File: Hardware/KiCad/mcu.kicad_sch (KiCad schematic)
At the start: 12 parts, among them U3 STM32F427ZGTx, Y1 8 MHz, Y2 32 kHz

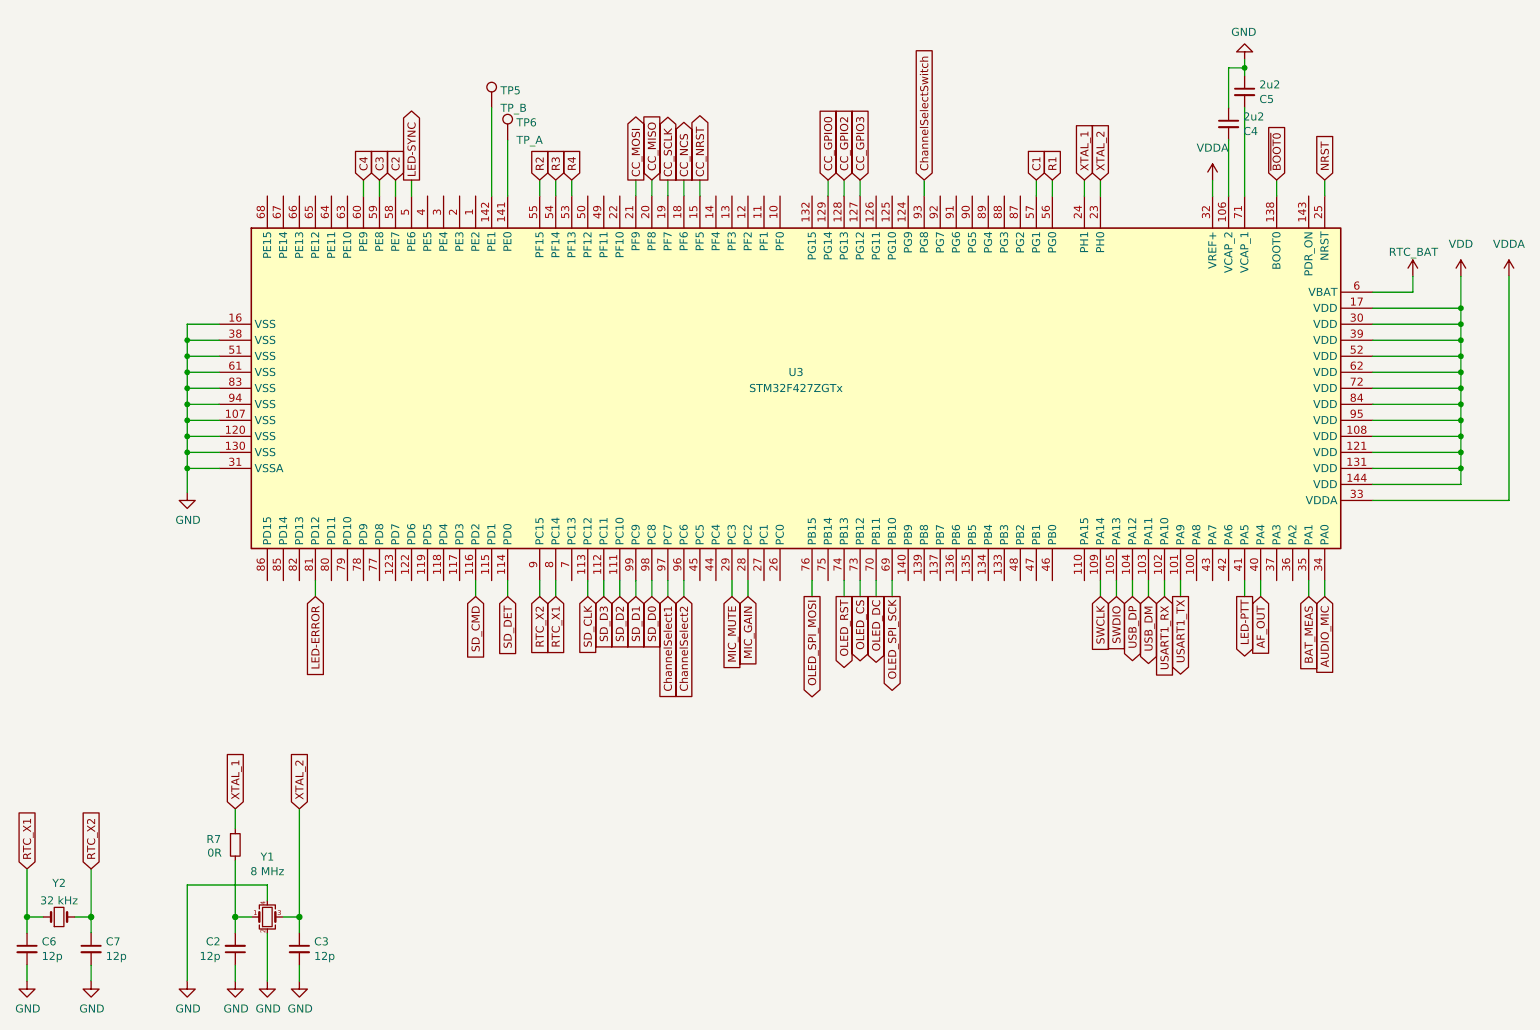
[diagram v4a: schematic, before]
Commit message: Schematic update
- nets for the internal speaker renamed
- encoder nets renamed, encoder circuit updated
- various other minor edits
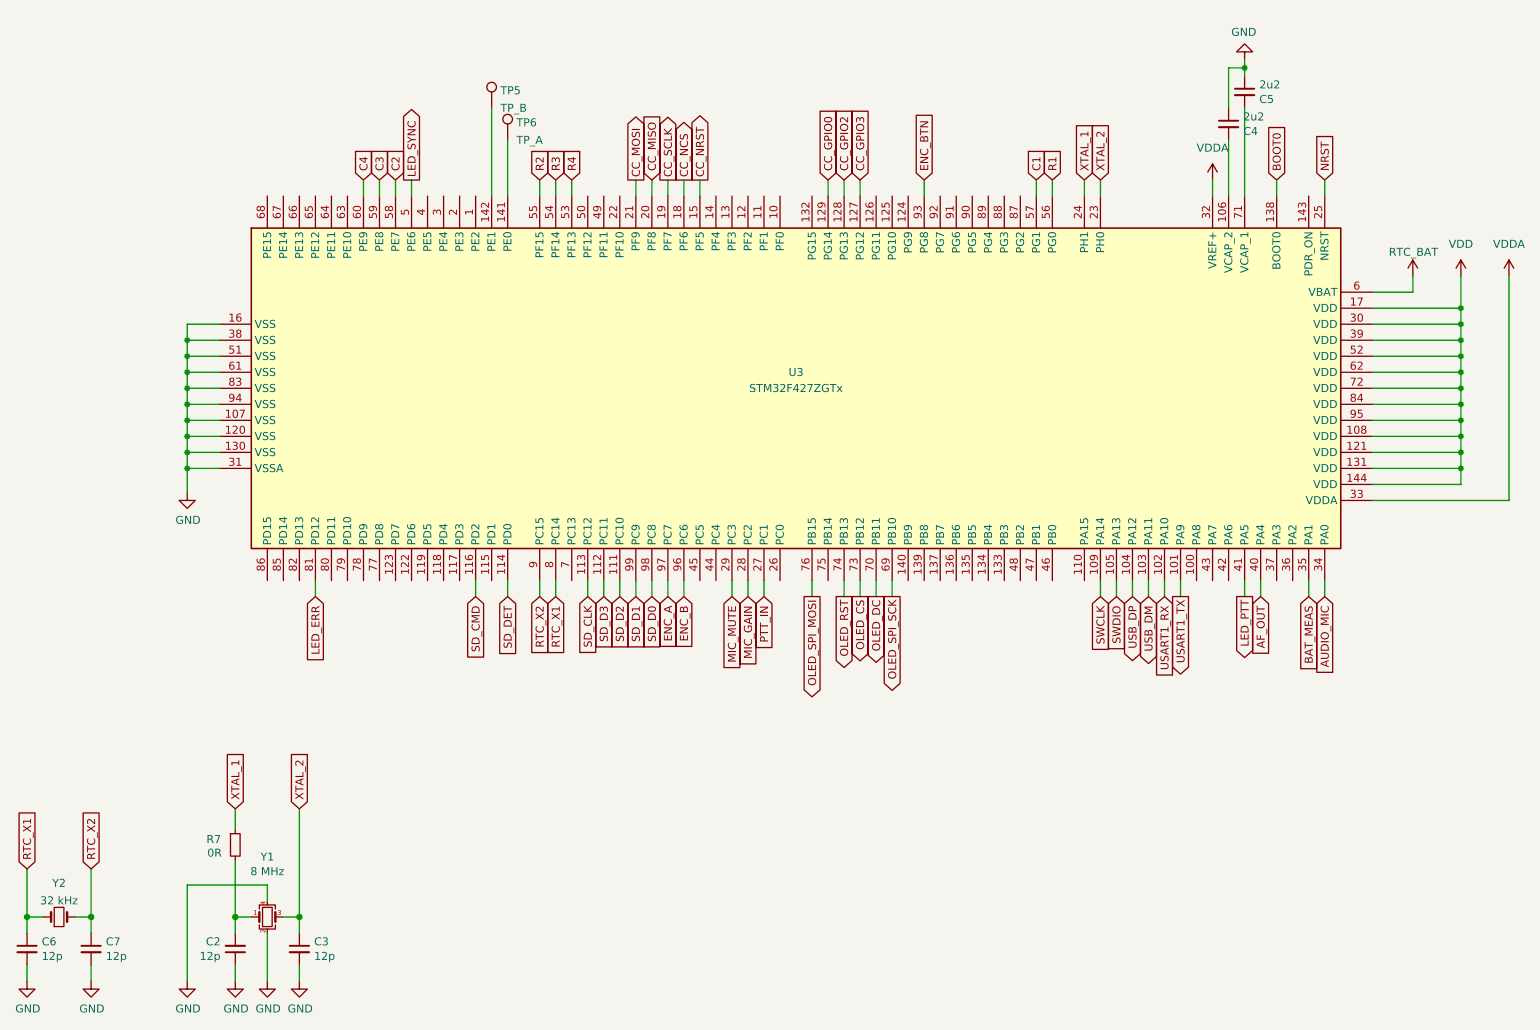
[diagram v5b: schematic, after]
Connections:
- net PTT_IN: now reaches U3.27 (PC1)
- net ChannelSelect1 renamed ENC_A
- net ChannelSelect2 renamed ENC_B
- net ChannelSelectSwitch renamed ENC_BTN
- net LED-ERROR renamed LED_ERR
- net LED-PTT renamed LED_PTT
- net LED-SYNC renamed LED_SYNC
- net ~{BOOT0} renamed BOOT0
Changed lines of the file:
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@@
+    (stroke (width 0) (type default) (color 0 0 0 0))
+  )
+  (wire (pts (xy 144.78 114.3) (xy 144.78 116.84))
     (stroke (width 0) (type default) (color 0 0 0 0))
   )
@@
     )
   )
-  (global_label "LED-SYNC" (shape output) (at 88.9 50.8 90) (fields_autoplaced)
-    (effects (font (size 1.27 1.27)) (justify left))
-    (property "Intersheet References" "${INTERSHEET_REFS}" (id 0) (at 88.8206 38.4688 90)
+  (global_label "LED_SYNC" (shape output) (at 88.9 50.8 90) (fields_autoplaced)
+    (effects (font (size 1.27 1.27)) (justify left))
+    (property "Intersheet References" "${INTERSHEET_REFS}" (id 0) (at 88.8206 39.0736 90)
       (effects (font (size 1.27 1.27)) (justify left) hide)
     )
@@
     )
   )
-  (global_label "LED-ERROR" (shape input) (at 73.66 116.84 270) (fields_autoplaced)
-    (effects (font (size 1.27 1.27)) (justify right))
-    (property "Intersheet References" "${INTERSHEET_REFS}" (id 0) (at -81.28 378.46 0)
-      (effects (font (size 1.27 1.27)) hide)
+  (global_label "LED_ERR" (shape input) (at 73.66 116.84 270) (fields_autoplaced)
+    (effects (font (size 1.27 1.27)) (justify right))
+    (property "Intersheet References" "${INTERSHEET_REFS}" (id 0) (at 73.5806 127.3569 90)
+      (effects (font (size 1.27 1.27)) (justify right) hide)
     )
   )
@@
     )
   )
-  (global_label "~{BOOT0}" (shape input) (at 226.06 50.8 90) (fields_autoplaced)
-    (effects (font (size 1.27 1.27)) (justify left))
-    (property "Intersheet References" "${INTERSHEET_REFS}" (id 0) (at 265.43 -19.05 0)
-      (effects (font (size 1.27 1.27)) hide)
+  (global_label "BOOT0" (shape input) (at 226.06 50.8 90) (fields_autoplaced)
+    (effects (font (size 1.27 1.27)) (justify left))
+    (property "Intersheet References" "${INTERSHEET_REFS}" (id 0) (at 225.9806 42.2788 90)
+      (effects (font (size 1.27 1.27)) (justify left) hide)
     )
   )
@@
     )
   )
-  (global_label "ChannelSelect1" (shape input) (at 129.54 116.84 270) (fields_autoplaced)
-    (effects (font (size 1.27 1.27)) (justify right))
-    (property "Intersheet References" "${INTERSHEET_REFS}" (id 0) (at 129.4606 133.9488 90)
+  (global_label "ENC_A" (shape input) (at 129.54 116.84 270) (fields_autoplaced)
+    (effects (font (size 1.27 1.27)) (justify right))
+    (property "Intersheet References" "${INTERSHEET_REFS}" (id 0) (at 129.4606 125.0588 90)
       (effects (font (size 1.27 1.27)) (justify right) hide)
     )
@@
     )
   )
-  (global_label "LED-PTT" (shape output) (at 220.98 116.84 270) (fields_autoplaced)
-    (effects (font (size 1.27 1.27)) (justify right))
-    (property "Intersheet References" "${INTERSHEET_REFS}" (id 0) (at 220.9006 127.4779 90)
+  (global_label "LED_PTT" (shape output) (at 220.98 116.84 270) (fields_autoplaced)
+    (effects (font (size 1.27 1.27)) (justify right))
+    (property "Intersheet References" "${INTERSHEET_REFS}" (id 0) (at 220.9006 126.8731 90)
       (effects (font (size 1.27 1.27)) (justify right) hide)
     )
@@
     )
   )
-  (global_label "ChannelSelect2" (shape input) (at 132.08 116.84 270) (fields_autoplaced)
-    (effects (font (size 1.27 1.27)) (justify right))
-    (property "Intersheet References" "${INTERSHEET_REFS}" (id 0) (at 132.0006 133.9488 90)
+  (global_label "ENC_B" (shape input) (at 132.08 116.84 270) (fields_autoplaced)
+    (effects (font (size 1.27 1.27)) (justify right))
+    (property "Intersheet References" "${INTERSHEET_REFS}" (id 0) (at 132.0006 125.2402 90)
       (effects (font (size 1.27 1.27)) (justify right) hide)
     )
@@
     )
   )
-  (global_label "ChannelSelectSwitch" (shape input) (at 170.18 50.8 90) (fields_autoplaced)
-    (effects (font (size 1.27 1.27)) (justify left))
-    (property "Intersheet References" "${INTERSHEET_REFS}" (id 0) (at 170.1006 28.7926 90)
+  (global_label "ENC_BTN" (shape input) (at 170.18 50.8 90) (fields_autoplaced)
+    (effects (font (size 1.27 1.27)) (justify left))
+    (property "Intersheet References" "${INTERSHEET_REFS}" (id 0) (at 170.1006 40.1017 90)
       (effects (font (size 1.27 1.27)) (justify left) hide)
     )
@@
     )
   )
+  (global_label "PTT_IN" (shape input) (at 144.78 116.84 270) (fields_autoplaced)
+    (effects (font (size 1.27 1.27)) (justify right))
+    (property "Intersheet References" "${INTERSHEET_REFS}" (id 0) (at 144.8594 125.3612 90)
+      (effects (font (size 1.27 1.27)) (justify right) hide)
+    )
+  )

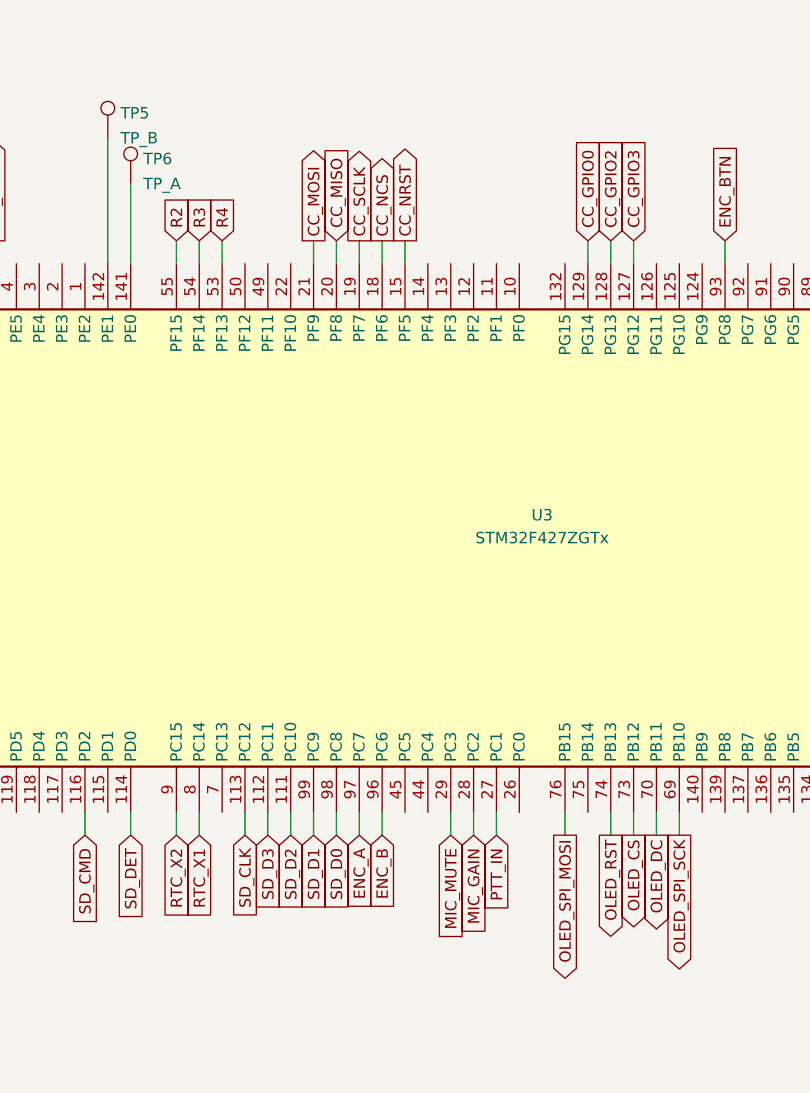
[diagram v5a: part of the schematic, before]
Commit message: Additional function buttons - F1, F2
Closes #24
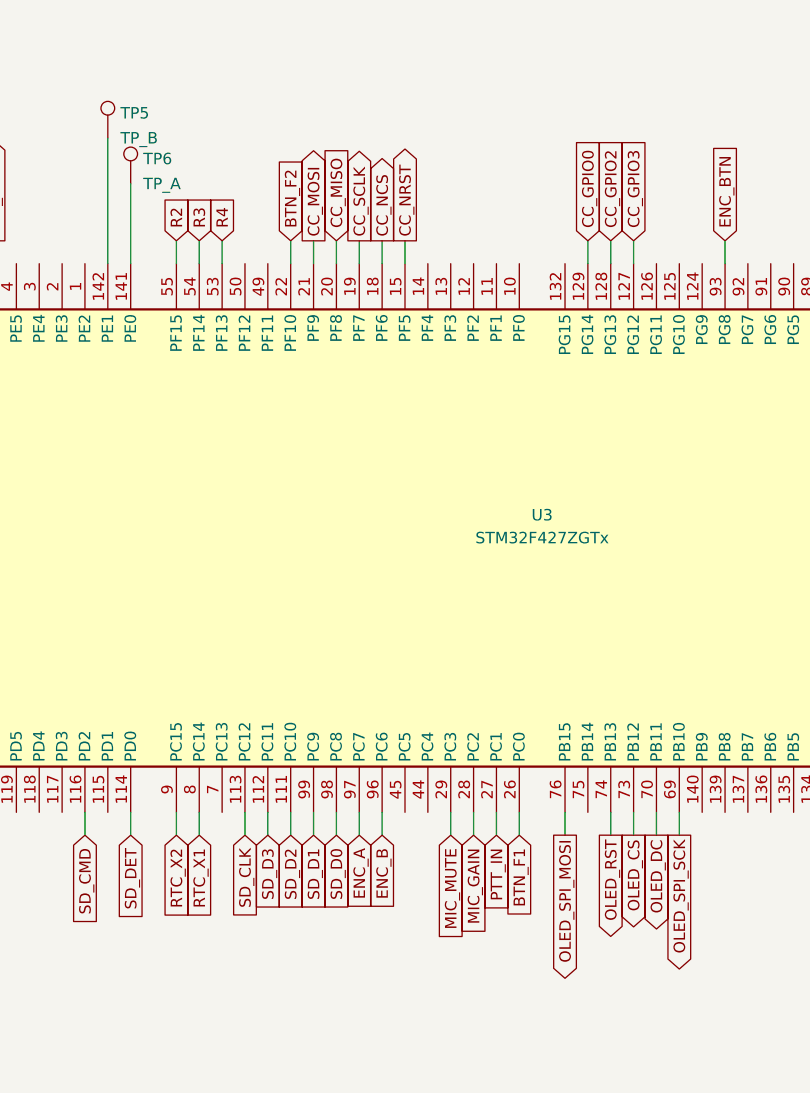
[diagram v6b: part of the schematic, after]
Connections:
- net BTN_F2: now reaches U3.22 (PF10)
- net BTN_F1: now reaches U3.26 (PC0)
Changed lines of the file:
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@@
+    (stroke (width 0) (type default) (color 0 0 0 0))
+  )
+  (wire (pts (xy 147.32 114.3) (xy 147.32 116.84))
     (stroke (width 0) (type default) (color 0 0 0 0))
   )
@@
     (stroke (width 0) (type default) (color 0 0 0 0))
   )
+  (wire (pts (xy 121.92 50.8) (xy 121.92 53.34))
+    (stroke (width 0) (type default) (color 0 0 0 0))
+  )
   (wire (pts (xy 241.3 76.2) (xy 255.27 76.2))
     (stroke (width 0) (type default) (color 0 0 0 0))
@@
     (effects (font (size 1.27 1.27)) (justify left))
     (property "Intersheet References" "${INTERSHEET_REFS}" (id 0) (at 134.5406 40.1017 90)
+      (effects (font (size 1.27 1.27)) (justify left) hide)
+    )
+  )
+  (global_label "BTN_F2" (shape input) (at 121.92 50.8 90) (fields_autoplaced)
+    (effects (font (size 1.27 1.27)) (justify left))
+    (property "Intersheet References" "${INTERSHEET_REFS}" (id 0) (at 121.8406 41.5531 90)
       (effects (font (size 1.27 1.27)) (justify left) hide)
     )
@@
       (effects (font (size 1.27 1.27)) (justify right) hide)
     )
+  )
+  (global_label "BTN_F1" (shape input) (at 147.32 116.84 270) (fields_autoplaced)
+    (effects (font (size 1.27 1.27)) (justify right))
+    (property "Intersheet References" "${INTERSHEET_REFS}" (id 0) (at 147.2406 126.0869 90)
+      (effects (font (size 1.27 1.27)) (justify right) hide)
+    )

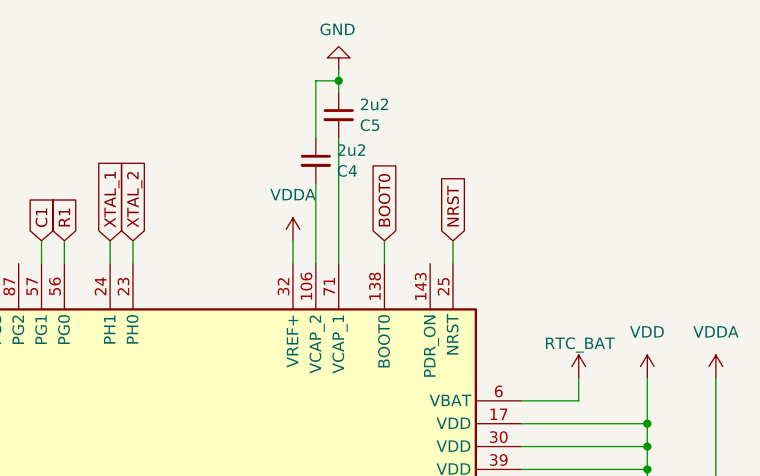
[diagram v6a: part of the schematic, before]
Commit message: add fpc display board connector, move components around, rough size of board
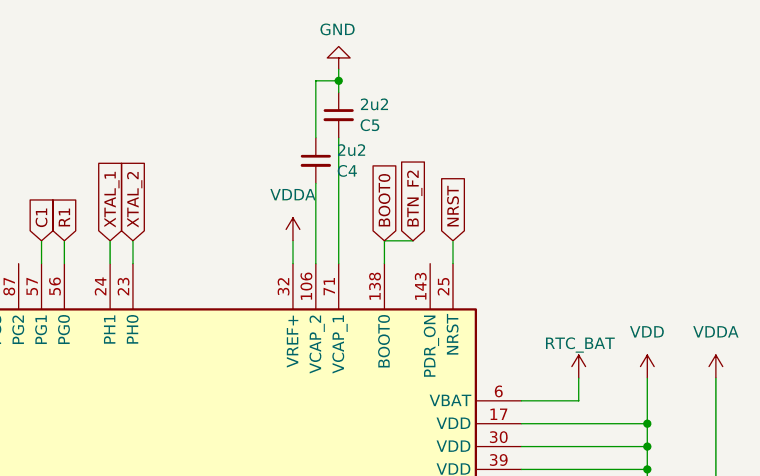
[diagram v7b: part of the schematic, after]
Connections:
- net BTN_F2 is gone; now on net BOOT0: U3.22 (PF10)
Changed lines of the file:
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@@
+    (stroke (width 0) (type default) (color 0 0 0 0))
+  )
+  (wire (pts (xy 226.06 50.8) (xy 229.235 50.8))
     (stroke (width 0) (type default) (color 0 0 0 0))
   )
@@
       (effects (font (size 1.27 1.27)) (justify left) hide)
     )
+  )
+  (global_label "BTN_F2" (shape input) (at 229.235 50.8 90) (fields_autoplaced)
+    (effects (font (size 1.27 1.27)) (justify left))
+    (property "Intersheet References" "${INTERSHEET_REFS}" (id 0) (at 229.1556 41.5531 90)
+      (effects (font (size 1.27 1.27)) (justify left) hide)
+    )
